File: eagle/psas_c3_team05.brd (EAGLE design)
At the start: 76.2 x 71.1 mm, 94 parts, among them IC1 CP2102, J1 3220-10-0100-00, J2 1.27MM_HDR_2X12X1, J4 1.27MM_HDR_2X12X1, U1 MIC5319 3.3V, U2 MCP73871, U3 MKW01Z128, X1 32 MHz

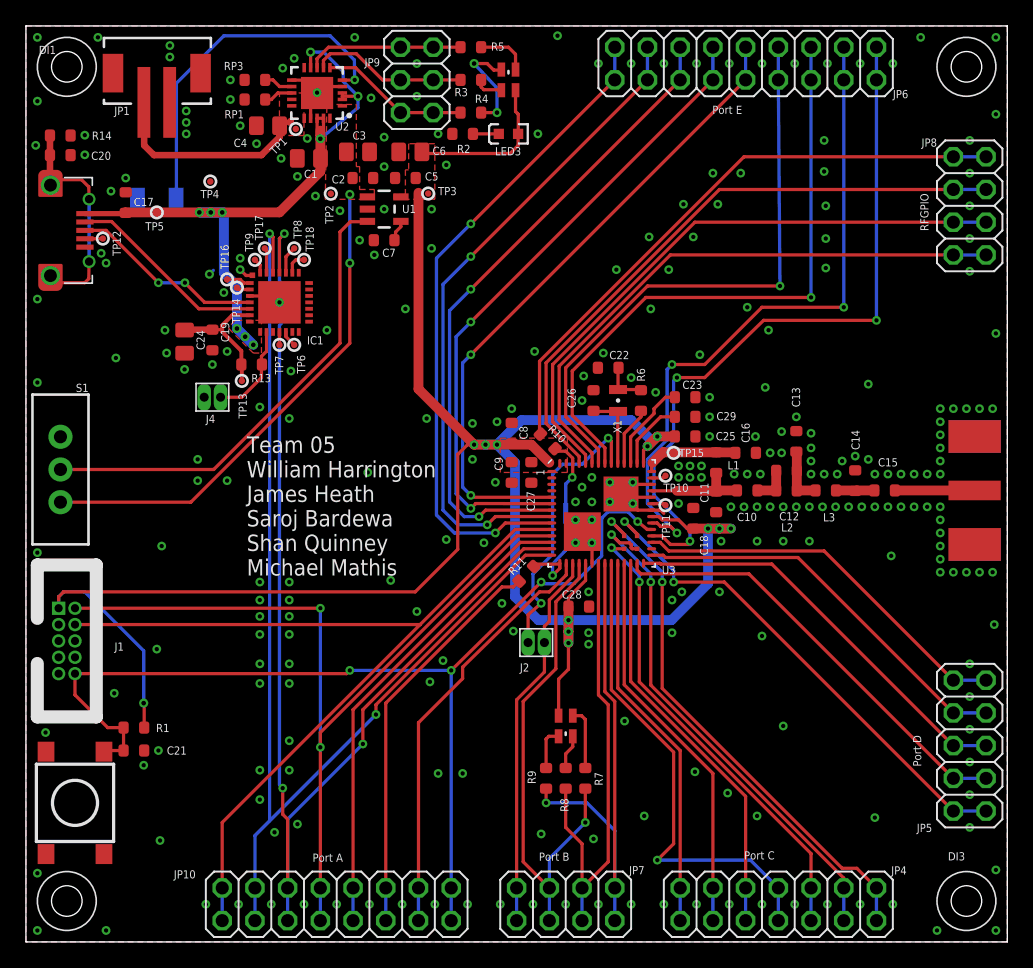
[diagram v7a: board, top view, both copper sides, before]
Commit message: Oh, and TSTOP ground clips for scope probes. And a VBAT jumper. And 3.3V jumper. All because debugging.
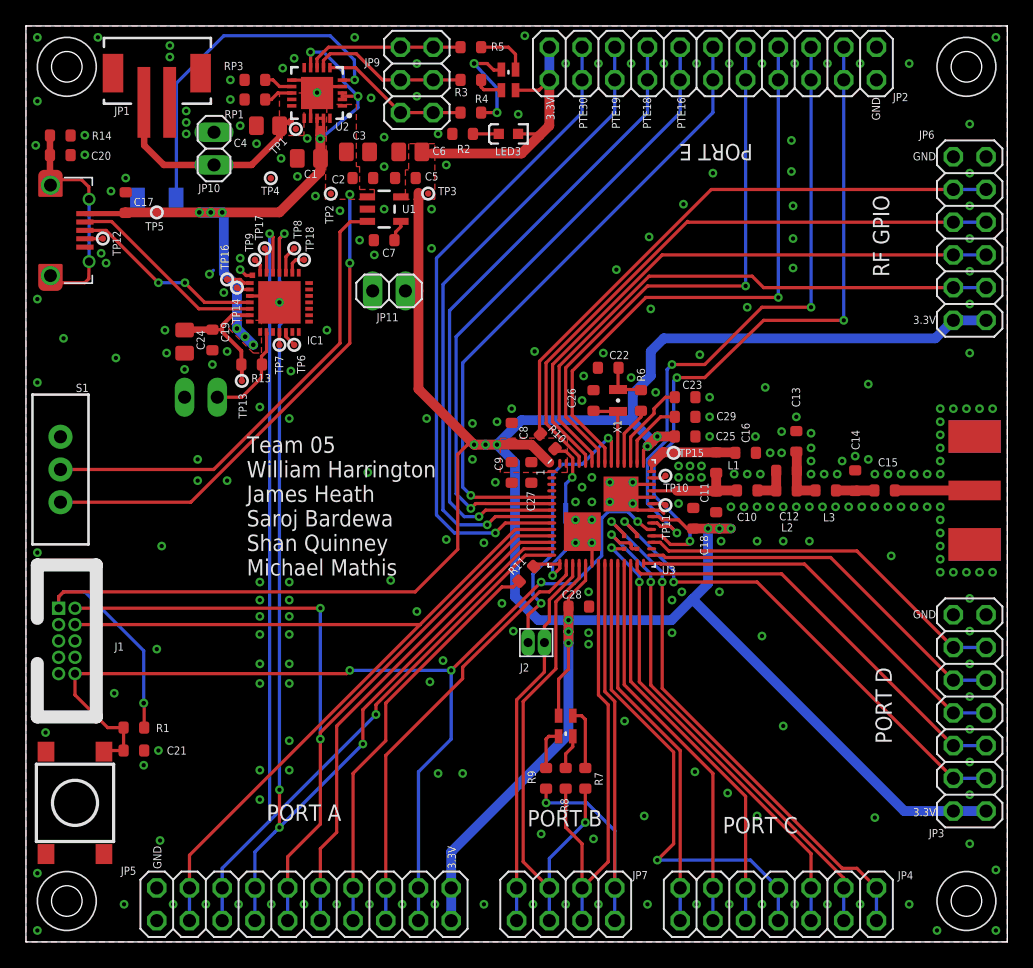
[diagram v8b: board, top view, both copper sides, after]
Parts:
- removed J4: 1.27MM_HDR_2X12X1, headers:1.27MM_2X1
- added JP11: (no value), pinhead:1X02
- added JP2: (no value), pinhead:2X11
- added JP3: (no value), pinhead:2X07
- JP10: device pinhead:2X08 -> pinhead:1X02
- JP5: device pinhead:2X05 -> pinhead:2X10
- JP6: device pinhead:2X09 -> pinhead:2X06
- JP8: device pinhead:2X04 -> pinhead:1X02
- moved JP8 61.5 mm to (13.6, 42.3), flipped to the bottom, turned to 0 degrees
- moved JP10 59.4 mm to (14.6, 61.6), turned to 90 degrees
- moved JP5 53.1 mm to (21.6, 2.92), turned to 0 degrees
- moved JP6 22.1 mm to (73.3, 54.6), turned to 90 degrees
- moved TP4 4.71 mm to (19.0, 59.3)
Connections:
- net 3.3V: now also JP11.1, JP2.21, JP2.22, JP3.1, JP3.2, JP5.19, JP5.20, JP6.1, JP6.2
- net DIO2: now also JP6.3, JP6.4; no longer JP8.1, JP8.2
- net DIO3: now also JP6.5, JP6.6; no longer JP8.3, JP8.4
- net DIO4: now also JP6.7, JP6.8; no longer JP8.5, JP8.6
- net DIO5-JMP: now also JP6.10, JP6.9; no longer JP8.7, JP8.8
- net GND: now also JP10.2, JP11.2, JP2.1, JP2.2, JP3.13, JP3.14, JP5.1, JP5.2, JP6.11, JP6.12, JP8.2; no longer J4.2
- net N$30: now also JP8.1; no longer J4.1
- net PTA0: now also JP5.3, JP5.4; no longer JP10.1, JP10.2
- net PTA1: now also JP5.5, JP5.6; no longer JP10.3, JP10.4
- net PTA18-JMP: now also JP5.13, JP5.14; no longer JP10.11, JP10.12
- net PTA19/XTAL0: now also JP5.15, JP5.16; no longer JP10.13, JP10.14
- net PTA2: now also JP5.7, JP5.8; no longer JP10.5, JP10.6
- net PTA20/!RESET: now also JP5.17, JP5.18; no longer JP10.15, JP10.16
- net PTA3: now also JP5.10, JP5.9; no longer JP10.7, JP10.8
- net PTA4: now also JP5.11, JP5.12; no longer JP10.10, JP10.9
- net PTD0: now also JP3.3, JP3.4; no longer JP5.1, JP5.2
- net PTD4: now also JP3.5, JP3.6; no longer JP5.3, JP5.4
- net PTD5: now also JP3.7, JP3.8; no longer JP5.5, JP5.6
- net PTD6: now also JP3.10, JP3.9; no longer JP5.7, JP5.8
- net PTD7: now also JP3.11, JP3.12; no longer JP5.10, JP5.9
- net PTE0: now also JP2.3, JP2.4; no longer JP6.1, JP6.2
- net PTE1: now also JP2.5, JP2.6; no longer JP6.3, JP6.4
- net PTE16: now also JP2.11, JP2.12; no longer JP6.10, JP6.9
- net PTE17: now also JP2.13, JP2.14; no longer JP6.11, JP6.12
- net PTE18: now also JP2.15, JP2.16; no longer JP6.13, JP6.14
- net PTE19: now also JP2.17, JP2.18; no longer JP6.15, JP6.16
- net PTE2: now also JP2.7, JP2.8; no longer JP6.5, JP6.6
- net PTE3: now also JP2.10, JP2.9; no longer JP6.7, JP6.8
- net PTE30: now also JP2.19, JP2.20; no longer JP6.17, JP6.18
- net V+: now also JP10.1
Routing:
- net 3.3V: track 174.6 -> 273.0 mm
- net PTA2: track 93.9 -> 90.0 mm, vias 3 -> 4
- net PTE3: track 46.3 -> 43.6 mm
- net PTE2: track 48.6 -> 46.0 mm
- net PTE0: track 56.6 -> 54.1 mm
- net PTE1: track 52.5 -> 49.9 mm
- net PTA0: track 69.4 -> 70.5 mm
- net PTA1: track 87.8 -> 88.9 mm
- net PTE16: track 50.5 -> 49.5 mm, vias 2 -> 1
- net PTD4: track 34.3 -> 33.3 mm
- net PTA4: track 37.2 -> 38.2 mm
- net PTD7: track 30.4 -> 29.3 mm
- net PTD6: track 31.0 -> 30.0 mm
- net PTD5: track 32.5 -> 31.4 mm
- net PTD0: track 39.4 -> 38.4 mm
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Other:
- board text added: "3.3V"
- board text added: "GND"
- board text added: "PORT A"
- board text added: "PORT B"
- board text added: "PORT C"
- board text added: "PORT D"
- board text added: "PORT E"
- board text added: "PTE16"
- board text added: "PTE18"
- board text added: "PTE19"
- board text added: "PTE30"
- board text added: "RF GPIO"
- board text removed: "Port A"
- board text removed: "Port B"
- board text removed: "Port C"
- board text removed: "Port D"
- board text removed: "Port E"
- board text removed: "RFGPIO"
